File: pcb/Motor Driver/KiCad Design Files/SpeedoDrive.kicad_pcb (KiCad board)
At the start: 2 copper layers, 22 x 34.3 mm, 20 parts, among them J1 Conn_01x05, J2 Conn_01x08, J3 Conn_01x06, J4 Conn_01x08, U1 VID6606

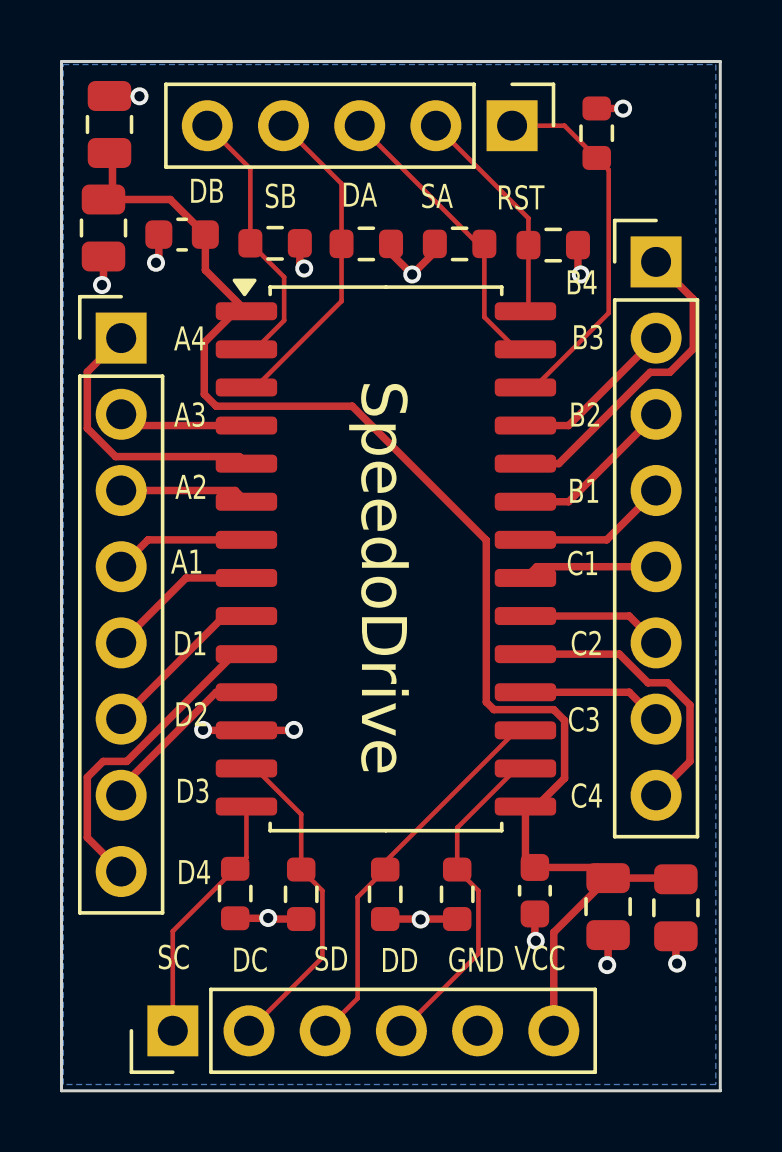
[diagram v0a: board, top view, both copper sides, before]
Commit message: Changes on kicad files for Motor Driver
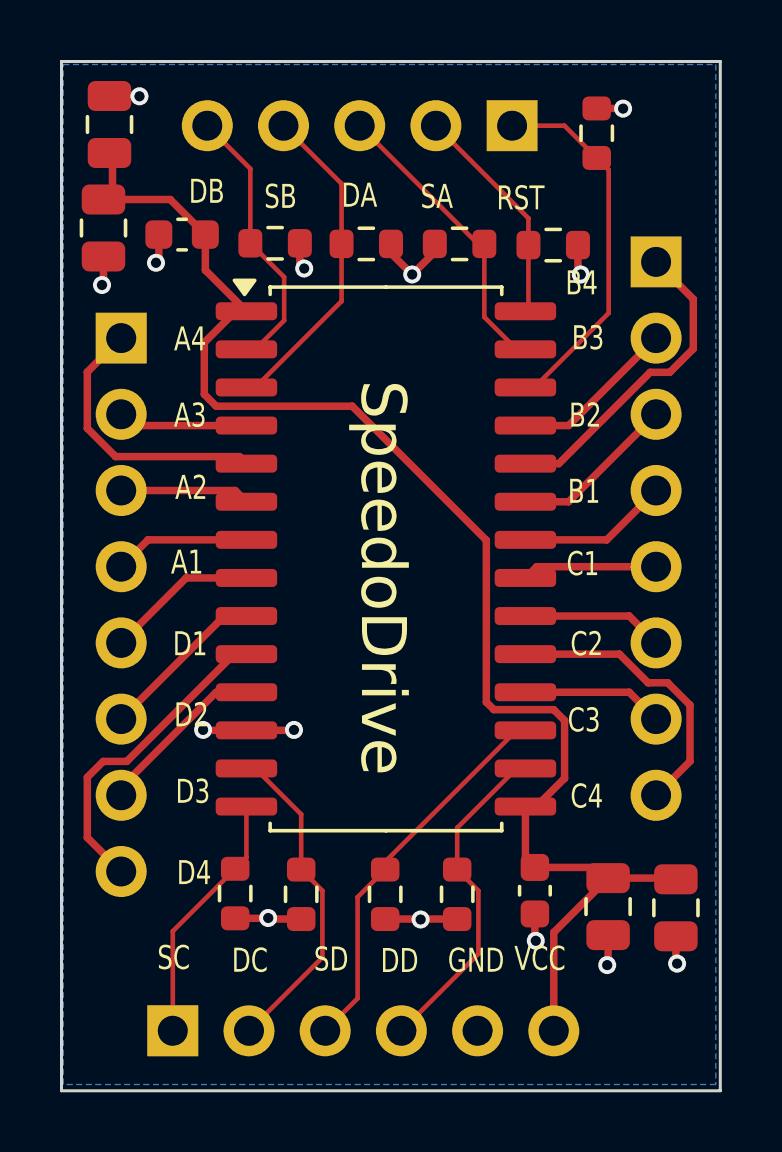
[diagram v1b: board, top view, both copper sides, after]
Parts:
- J1, J2, J3, J4: moved to B.Cu
- turned J1 to 90 degrees
- turned J2 to 180 degrees
- turned J3 to -90 degrees
- turned J4 to 180 degrees
